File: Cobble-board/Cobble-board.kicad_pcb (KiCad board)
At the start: 2 copper layers, 42 x 45 mm, 5 parts

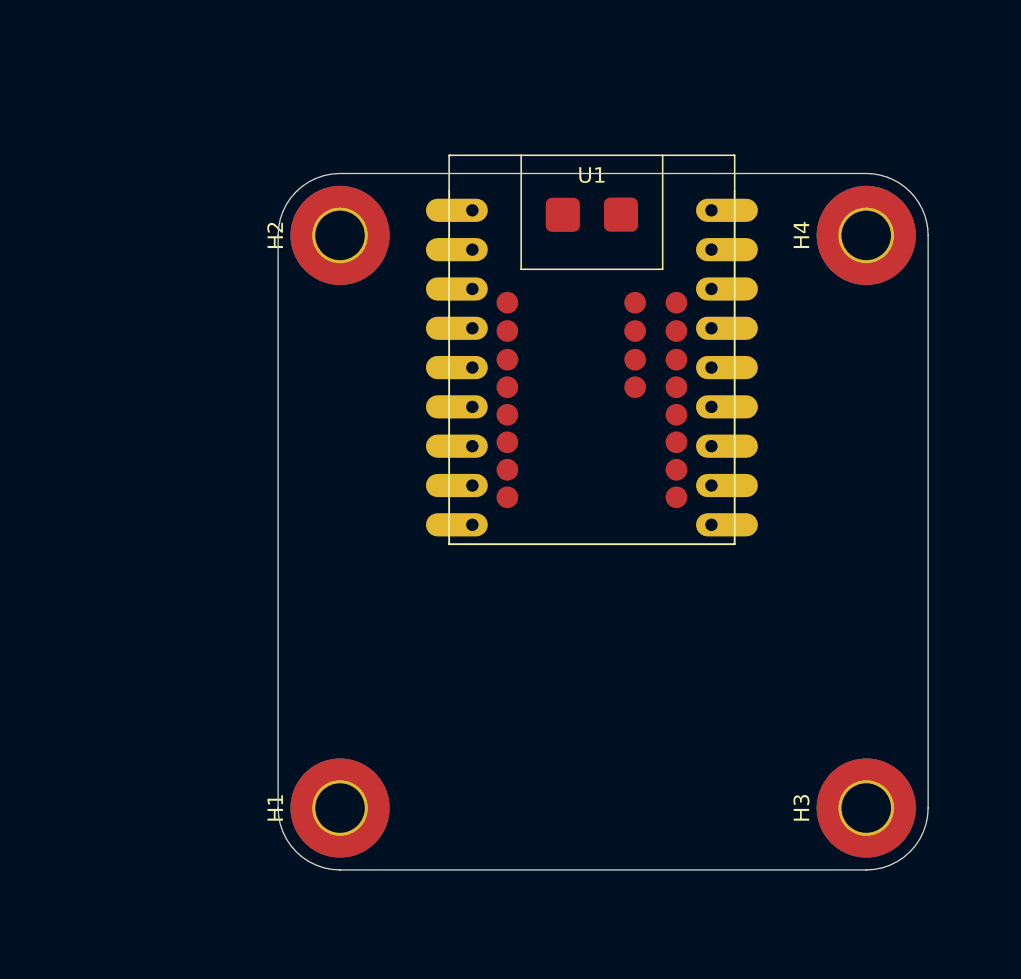
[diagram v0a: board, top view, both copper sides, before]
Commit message: added most components.  waiting on clarification for speaker and i2c connectors
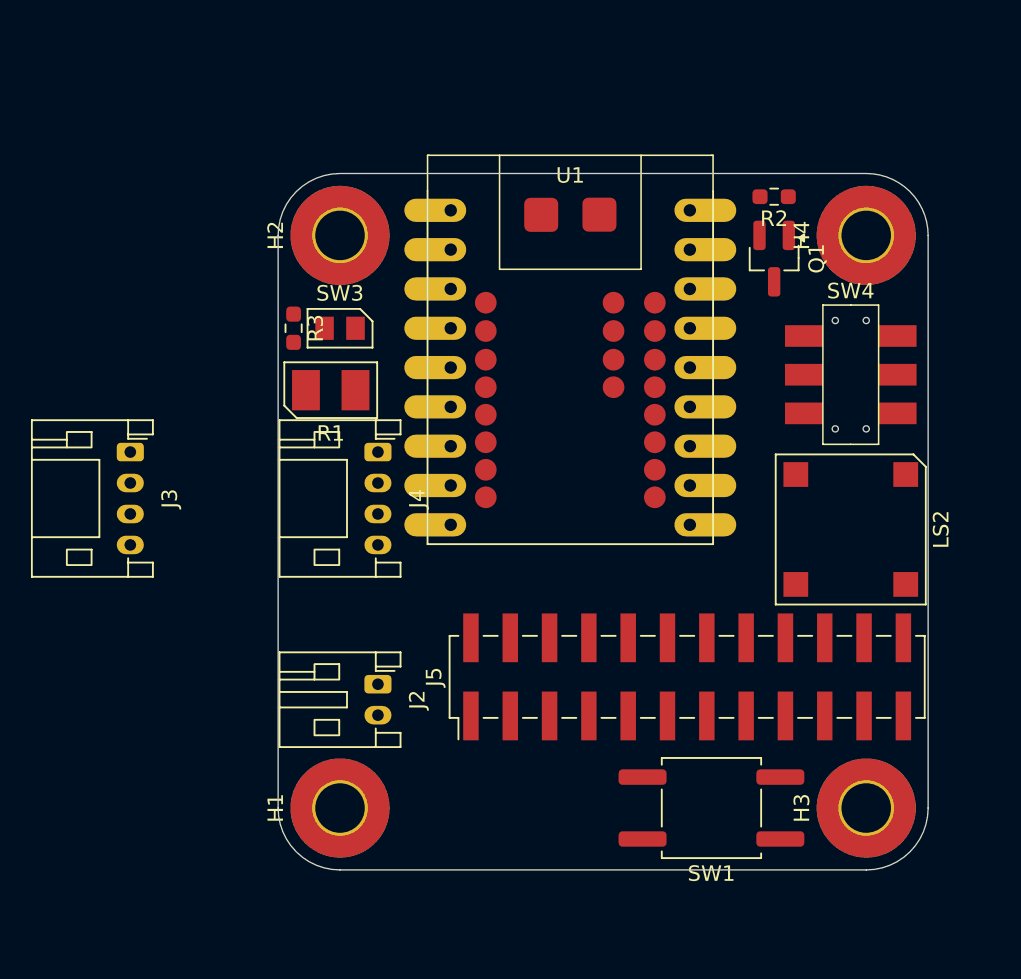
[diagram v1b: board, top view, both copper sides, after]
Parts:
- added J2: JST PH2.0 Battery, Connector_JST:JST_PH_S2B-PH-K_1x02_P2.00mm_Horizontal, F.Cu at (18.4, 45.0)
- added J3: Stemma PH, Connector_JST:JST_PH_S4B-PH-K_1x04_P2.00mm_Horizontal, F.Cu at (2.45, 30.0)
- added J4: Grove, Connector_JST:JST_PH_S4B-PH-K_1x04_P2.00mm_Horizontal, F.Cu at (18.4, 30.0)
- added J5: Conn_02x12_Odd_Even, Connector_PinHeader_2.54mm:PinHeader_2x12_P2.54mm_Vertical_SMD, F.Cu at (38.4, 44.5)
- added LS2: MLT-8530, Cobble_Library:MLT-8530, F.Cu at (49.0, 35.0)
- added Q1: SI2302DS, Package_TO_SOT_SMD:SOT-23_Handsoldering, F.Cu at (44.0, 17.5)
- added R1: GT36528, Cobble_Library:GT36528, F.Cu at (15.4, 26.0)
- added R2: 1M, Resistor_SMD:R_0603_1608Metric_Pad0.98x0.95mm_HandSolder, F.Cu at (44.1, 13.5)
- added R3: 10k, Resistor_SMD:R_0603_1608Metric_Pad0.98x0.95mm_HandSolder, F.Cu at (13.0, 22.0)
- added SW1: SW_Push, Button_Switch_SMD:SW_Push_1P1T_NO_CK_KSC6xxG, F.Cu at (40.0, 53.0)
- added SW3: SW_VIBE, Cobble_Library:X160, F.Cu at (16.0, 22.0)
- added SW4: MSK22D27, Cobble_Library:MSK22D27, F.Cu at (49.0, 25.0)
- moved U1 1.40 mm to (30.9, 24.5)
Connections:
- U1 pad 16: unconnected-(U1-3V3-Pad16) -> +3V3
- U1 pad 17: unconnected-(U1-GND-Pad17) -> GND
- U1 pad 18: unconnected-(U1-5V-Pad18) -> +5V
- U1 pad 3: unconnected-(U1-GPIO1-Pad3) -> Buzzer
- U1 pad 39: unconnected-(U1-B+-Pad39) -> VBatt_SW
- U1 pad 4: unconnected-(U1-GPIO2-Pad4) -> LightSense
- U1 pad 40: unconnected-(U1-B--Pad40) -> GND
- U1 pad 5: unconnected-(U1-GPIO3-Pad5) -> PushButton
- U1 pad 6: unconnected-(U1-GPIO4-Pad6) -> VibeSense

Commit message: main PWB is nearly complete.  need to add logo and fix one rat line.  added a cobble-board-test for a simpler single sided fab test board
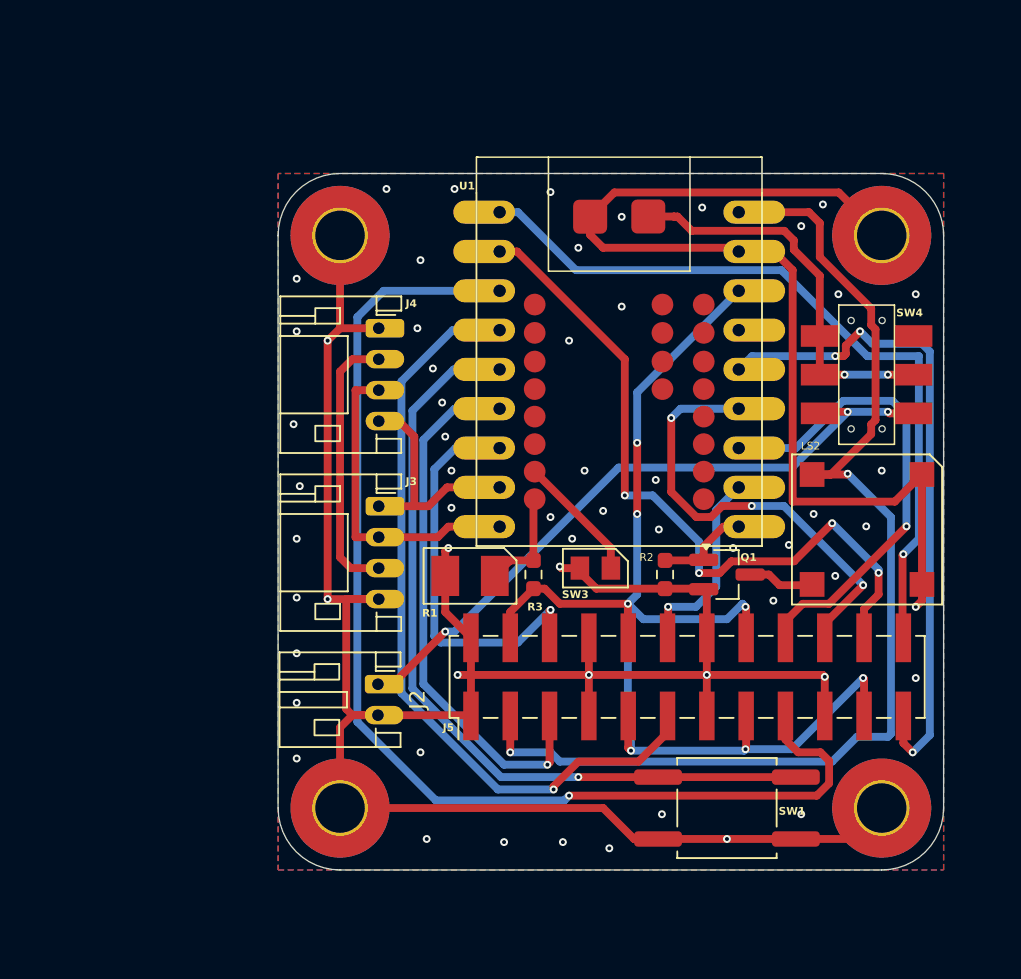
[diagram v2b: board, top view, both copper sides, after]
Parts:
- J2: footprint Connector_JST:JST_PH_S2B-PH-K_1x02_P2.00mm_Horizontal -> Cobble_Library:Battery_1x02_P2.00mm_Horizontal
- J3, J4: footprint Connector_JST:JST_PH_S4B-PH-K_1x04_P2.00mm_Horizontal -> Cobble_Library:Stemma_Grove_1x04_P2.00mm_Horizontal
- moved R2 25.4 mm to (37.0, 37.9), turned to -90 degrees
- moved SW3 22.6 mm to (32.5, 37.5)
- moved R3 22.2 mm to (28.5, 37.9), turned to 90 degrees
- moved Q1 20.6 mm to (41.0, 37.9), turned to 0 degrees
- moved J3 16.4 mm to (18.5, 33.5)
- moved R1 15.0 mm to (24.4, 38.0), turned to 180 degrees
- moved J4 8.00 mm to (18.5, 22.0)
- moved U1 3.16 mm to (34.0, 24.7)
- moved LS2 1.05 mm to (50.0, 35.0)
- moved SW4 1.02 mm to (50.0, 25.0)
- moved H4 1.00 mm to (51.0, 16.0)
- moved SW1 1.00 mm to (41.0, 53.0)
- moved H3 1.00 mm to (51.0, 53.0)
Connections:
- J3 pad 3: +3V3 -> 3V3
- J4 pad 2: +3V3 -> 3V3
- J5 pad 1: unconnected-(J5-Pin_1-Pad1) -> GND
- J5 pad 10: unconnected-(J5-Pin_10-Pad10) -> 3V3
- J5 pad 11: unconnected-(J5-Pin_11-Pad11) -> GPIO2
- J5 pad 12: unconnected-(J5-Pin_12-Pad12) -> GPIO9
- J5 pad 13: unconnected-(J5-Pin_13-Pad13) -> GND
- J5 pad 14: unconnected-(J5-Pin_14-Pad14) -> GND
- J5 pad 15: unconnected-(J5-Pin_15-Pad15) -> 3V3
- J5 pad 16: unconnected-(J5-Pin_16-Pad16) -> 3V3
- J5 pad 17: unconnected-(J5-Pin_17-Pad17) -> GPIO1
- J5 pad 18: unconnected-(J5-Pin_18-Pad18) -> GPIO10
- J5 pad 19: unconnected-(J5-Pin_19-Pad19) -> GND
- J5 pad 2: unconnected-(J5-Pin_2-Pad2) -> GND
- J5 pad 20: unconnected-(J5-Pin_20-Pad20) -> GPIO11
- J5 pad 21: unconnected-(J5-Pin_21-Pad21) -> 3V3
- J5 pad 22: unconnected-(J5-Pin_22-Pad22) -> RXD-GPIO44
- J5 pad 23: unconnected-(J5-Pin_23-Pad23) -> GPIO12
- J5 pad 24: unconnected-(J5-Pin_24-Pad24) -> TXD-GPIO43
- J5 pad 3: unconnected-(J5-Pin_3-Pad3) -> VBUS
- J5 pad 4: unconnected-(J5-Pin_4-Pad4) -> 3V3
- J5 pad 5: unconnected-(J5-Pin_5-Pad5) -> GPIO4
- J5 pad 6: unconnected-(J5-Pin_6-Pad6) -> GPIO5
- J5 pad 7: unconnected-(J5-Pin_7-Pad7) -> GND
- J5 pad 8: unconnected-(J5-Pin_8-Pad8) -> GND
- J5 pad 9: unconnected-(J5-Pin_9-Pad9) -> 3V3
- LS2 pad 1: +5V -> VBUS
- R3 pad 1: +3V3 -> 3V3
- SW4 pad 1: unconnected-(SW4-A-Pad1) -> VBatt_SW
- U1 pad 1: unconnected-(U1-TXD-Pad1) -> TXD-GPIO43
- U1 pad 10: unconnected-(U1-GPIO8-Pad10) -> Buzzer
- U1 pad 11: unconnected-(U1-GPIO9-Pad11) -> GPIO9
- U1 pad 12: unconnected-(U1-GPIO10-Pad12) -> GPIO10
- U1 pad 13: unconnected-(U1-GPIO11-Pad13) -> GPIO11
- U1 pad 14: unconnected-(U1-GPIO12-Pad14) -> GPIO12
- U1 pad 15: unconnected-(U1-GPIO13-Pad15) -> GPIO13
- U1 pad 16: +3V3 -> 3V3
- U1 pad 18: +5V -> VBUS
- U1 pad 2: unconnected-(U1-RXD-Pad2) -> RXD-GPIO44
- U1 pad 25: unconnected-(U1-GPIO40-Pad25) -> VibeSense
- U1 pad 26: unconnected-(U1-GPIO39-Pad26) -> LightSense
- U1 pad 3: Buzzer -> GPIO1
- U1 pad 4: LightSense -> GPIO2
- U1 pad 6: VibeSense -> GPIO4
- U1 pad 7: unconnected-(U1-GPIO5-Pad7) -> GPIO5
- U1 pad 8: unconnected-(U1-GPIO6-Pad8) -> SCL
- U1 pad 9: unconnected-(U1-GPIO7-Pad9) -> SDA
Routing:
- net GND: track 0.00 -> 221.6 mm, vias 0 -> 59
- net 3V3: track 0.00 -> 97.3 mm, vias 0 -> 7
- net GPIO1: track 0.00 -> 75.5 mm, vias 0 -> 1
- net VBUS: track 0.00 -> 73.9 mm, vias 0 -> 2
- net PushButton: track 0.00 -> 51.8 mm, vias 0 -> 1
- net GPIO2: track 0.00 -> 50.3 mm, vias 0 -> 1
- net TXD-GPIO43: track 0.00 -> 49.6 mm, vias 0 -> 1
- net RXD-GPIO44: track 0.00 -> 46.8 mm, vias 0 -> 4
- net Net-(J2-Pin_1): track 0.00 -> 43.8 mm, vias 0 -> 3
- net GPIO12: track 0.00 -> 43.2 mm, vias 0 -> 3
- net GPIO4: track 0.00 -> 34.9 mm, vias 0 -> 1
- net GPIO10: track 0.00 -> 31.1 mm, vias 0 -> 1
- net GPIO11: track 0.00 -> 29.3 mm, vias 0 -> 3
- net GPIO5: track 0.00 -> 26.0 mm, vias 0 -> 1
- net VBatt_SW: track 0.00 -> 25.5 mm, vias 0 -> 2
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- added copper zone on B.Cu, net GND
- added copper zone on F.Cu, net GND
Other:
- board size 42 x 45 mm -> 43 x 45 mm

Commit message: Cobbl-board-test is complete and tested
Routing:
- net GND: vias 59 -> 94
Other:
- board text added: "+ -"
- board text added: "Find the Docs! cobble.tinkerfarm.net"
- board text added: "WildCircuits | Tinkerfarm.net | Brockport Original Builds"

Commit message: Cobble schematic is updated with changes identified from Cobble-board-test. issues fixed: vibe sensor pad too small, SW1 pin spacing wrong, light sensor wired to non-ADC pin, 4 spins on ADC header for SPI, missing I2C pullup resistors, light sensor R shoudl be smaller (10K), SW4 alignment holes too small, ESP32S3 footprint didn't have battery charge boost pads
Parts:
- added R4: 4k7, Resistor_SMD:R_0603_1608Metric_Pad0.98x0.95mm_HandSolder, F.Cu at (19.9, 5.25)
- added R5: 4k7, Resistor_SMD:R_0603_1608Metric_Pad0.98x0.95mm_HandSolder, F.Cu at (19.9, 7.76)
- SW1: footprint Button_Switch_SMD:SW_Push_1P1T_NO_CK_KSC6xxG -> Cobble_Library:SW_Push_1P1T
- U1: footprint Cobble_Library:ESP32S3-supermini -> Cobble_Library:ESP32S3-supermini-v2
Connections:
- J5 pad 11: GPIO2 -> GPIO1
- J5 pad 17: GPIO1 -> GPIO2
- J5 pad 18: GPIO10 -> GPIO13
- J5 pad 20: GPIO11 -> GPIO12
- J5 pad 22: RXD-GPIO44 -> GPIO11
- J5 pad 23: GPIO12 -> GPIO4
- J5 pad 24: TXD-GPIO43 -> GPIO10
- J5 pad 5: GPIO4 -> TXD-GPIO43
- J5 pad 6: GPIO5 -> RXD-GPIO44
- U1 pad 26: LightSense -> unconnected-(U1-GPIO39-Pad26)
- U1 pad 7: GPIO5 -> LightSense
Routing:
- net GPIO5: track 26.0 -> 0.00 mm, vias 1 -> 0
- net (no net): track 0.00 -> 26.0 mm
- net LightSense: vias 0 -> 1
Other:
- board text added: "Cobble"

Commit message: Cobble board is rev 1 is ready for review
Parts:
- J2: footprint Cobble_Library:Battery_1x02_P2.00mm_Horizontal -> Connector_JST:JST_PH_B2B-PH-SM4-TB_1x02-1MP_P2.00mm_Vertical
- J3: footprint Cobble_Library:Stemma_Grove_1x04_P2.00mm_Horizontal -> Connector_JST:JST_PH_B4B-PH-SM4-TB_1x04-1MP_P2.00mm_Vertical
- J4: footprint Cobble_Library:Stemma_Grove_1x04_P2.00mm_Horizontal -> Grove:GROVE-HW4-SMD-2.0
- moved R4 12.9 mm to (22.2, 17.9), turned to 90 degrees
- moved R5 10.2 mm to (20.2, 17.9), turned to 90 degrees
- moved SW3 6.29 mm to (38.8, 38.2), turned to 0 degrees
- moved R1 5.46 mm to (29.9, 38.2), turned to 0 degrees
- moved R2 4.51 mm to (41.5, 38.2)
- moved Q1 4.26 mm to (45.2, 38.2)
- moved R3 3.38 mm to (25.2, 37.0), turned to 0 degrees
- moved SW4 3.04 mm to (53.0, 24.5)
- moved H3 3.00 mm to (54.0, 53.0)
- moved H4 3.00 mm to (54.0, 16.0)
- moved J5 3.00 mm to (41.4, 44.5)
- moved LS2 3.00 mm to (53.0, 35.0)
- moved SW1 3.00 mm to (44.0, 53.0)
- moved U1 2.94 mm to (37.0, 24.8)
- moved J3 2.14 mm to (19.2, 31.5), turned to 180 degrees
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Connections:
- J5 pad 11: GPIO1 -> GPIO2
- J5 pad 12: GPIO9 -> GPIO15
- J5 pad 17: GPIO2 -> GPIO4
- J5 pad 18: GPIO13 -> GPIO10
- J5 pad 20: GPIO12 -> GPIO11
- J5 pad 22: GPIO11 -> GPIO12
- J5 pad 23: GPIO4 -> GPIO5
- J5 pad 24: GPIO10 -> GPIO13
- J5 pad 5: TXD-GPIO43 -> GPIO1
- J5 pad 6: RXD-GPIO44 -> GPIO6
- U1 pad 1: TXD-GPIO43 -> TXD
- U1 pad 11: GPIO9 -> VibeSense
- U1 pad 2: RXD-GPIO44 -> RXD
- U1 pad 25: VibeSense -> unconnected-(U1-GPIO40-Pad25)
- U1 pad 28: unconnected-(U1-GPIO15-Pad28) -> GPIO15
- U1 pad 29: unconnected-(U1-GPIO16-Pad29) -> SCL
- U1 pad 30: unconnected-(U1-GPIO17-Pad30) -> SDA
- U1 pad 35: unconnected-(U1-GPIO35-Pad35) -> PushButton
- U1 pad 5: PushButton -> unconnected-(U1-GPIO3-Pad5)
- U1 pad 7: LightSense -> GPIO5
- U1 pad 8: SCL -> GPIO6
- U1 pad 9: SDA -> LightSense
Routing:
- net GND: track 221.6 -> 22.6 mm, vias 94 -> 100
- net GPIO5: track 0.00 -> 52.8 mm, vias 0 -> 1
- net TXD-GPIO43: track 49.6 -> 0.00 mm, vias 1 -> 0
- net RXD-GPIO44: track 46.8 -> 0.00 mm, vias 4 -> 0
- net GPIO1: track 75.5 -> 45.3 mm, vias 1 -> 2
- net GPIO13: track 0.00 -> 28.3 mm, vias 0 -> 2
- net (no net): track 26.0 -> 0.00 mm
- net GPIO4: track 34.9 -> 59.0 mm
- net GPIO12: track 43.2 -> 22.4 mm, vias 3 -> 0
- net Net-(J2-Pin_1): track 43.8 -> 64.0 mm, vias 3 -> 2
- net 3V3: track 97.3 -> 115.7 mm, vias 7 -> 2
- net SCL: track 15.5 -> 33.2 mm, vias 0 -> 2
- net GPIO15: track 0.00 -> 17.0 mm
- net SDA: track 20.6 -> 36.6 mm, vias 0 -> 2
- net GPIO10: track 31.1 -> 17.7 mm, vias 1 -> 0
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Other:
- board size 43 x 45 mm -> 46 x 45 mm
- board text added: "Tinkerfarm.net X WildCircuits X Brockport Original Builds"
- board text removed: "WildCircuits | Tinkerfarm.net | Brockport Original Builds"

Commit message: Rev 1 released for fab at OSHPark
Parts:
- added R6: 4k7, Resistor_THT:R_Axial_DIN0204_L3.6mm_D1.6mm_P5.08mm_Horizontal, F.Cu at (22.8, 18.4)
- added R7: 4k7, Resistor_THT:R_Axial_DIN0204_L3.6mm_D1.6mm_P5.08mm_Horizontal, F.Cu at (20.6, 18.4)
- moved R4 2.27 mm to (22.8, 15.7)
- moved R5 2.06 mm to (20.6, 15.9)
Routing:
- net 3V3: track 115.7 -> 122.9 mm
- net GND: track 22.6 -> 29.5 mm
- net VBatt_SW: track 26.7 -> 32.9 mm
- net SCL: track 33.2 -> 35.7 mm
- net SDA: track 36.6 -> 38.8 mm
- net GPIO5: track 52.8 -> 51.4 mm
- net GPIO2: track 51.8 -> 53.2 mm
- net GPIO4: track 59.0 -> 60.2 mm
- net GPIO1: track 45.3 -> 46.3 mm
- net GPIO13: track 28.3 -> 29.2 mm
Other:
- board text added: "3.3V"
- board text added: "GND"
- board text added: "Header Pinout"
- board text added: "IO1"
- board text added: "IO10"
- board text added: "IO11"
- board text added: "IO12"
- board text added: "IO13"
- board text added: "IO15"
- board text added: "IO2"
- board text added: "IO4"
- board text added: "IO5"
- board text added: "IO6"
- board text added: "Rev 1 10/27/2026"
- board text added: "See bottom for full pinout"
- board text added: "VBUS"
- board text removed: "Cobble"
